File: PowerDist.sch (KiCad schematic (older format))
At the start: 15 parts, among them J3 CarPowerConnector, U2 RI3-1205S, U3 NCP1117-3.3_SOT223

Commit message: Updates dashboard project to most recent version
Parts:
- removed C16: 470pF, Capacitor_SMD:C_2220_5650Metric, symbol Device:C
- removed J3: CarPowerConnector, UTSVT_Connectors:Molex_MicroFit3.0_1x2xP3.00mm_PolarizingPeg_Vertical, symbol utsvt-connectors:CarPowerConnector
- removed L4: SRF0905-100Y, UTSVT_BPS:SRF0905A, symbol utsvt-bps:SRF0905-100Y
- added J18: PowerConn, UTSVT_Connectors:Molex_MicroFit3.0_1x2xP3.00mm_PolarizingPeg_Vertical, symbol Connector_Generic:Conn_01x02
- C20: renamed from C14; value 4.7uF -> 10u; footprint Capacitor_SMD:C_0805_2012Metric -> UTSVT_Passive:C_2220_5750Metric
- C21: renamed from C15; value 0.1uF -> 10u
- C22: renamed from C17; value 10uF -> 10u
- renumbered D1 to D14, R1 to R29, TP1 to TP2, TP2 to TP3, TP3 to TP4, TP4 to TP5, TP5 to TP6, U2 to U12, U3 to U13
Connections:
- wire segments 60 -> 57
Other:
- note added: "+5V is already isolated so no need to isolate +3.3V"
- note added: "ISOLATED"
- note added: "Isolated DC-DC Converter to step down +12V power\nto an isolated +5V. The input gnd (Power GND) is\ndifferent from the output gnd (Local GND)"
- note added: "Linear Regulator to step down +5V to +3.3V.\nAn isolated converter was not used for the +3.3V\nline because of price and space. May need to\nchange this to DC-DC converter if we really\nwant to make the BPS more energy efficient."
- note added: "Local (Leader Board) GND\n(Internal)"
- note added: "Power GND\n(External)"
- note removed: "Two separate converters would cause more noise on the board but less power waste.\nIf too much noise, add 5 to 3.3V regulator.\n"
- moved on the sheet: C20, C21, C22, D14, R29, TP2, TP3, TP4, TP5, TP6, U13

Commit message: Edits schematic to make turn lights software controlled
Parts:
- TP2, TP3, TP4, TP5, TP6: footprint TestPoint:TestPoint_Keystone_5005-5009_Compact -> TestPoint:TestPoint_Pad_1.5x1.5mm
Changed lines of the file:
@@
 $Descr A4 11693 8268
 encoding utf-8
-Sheet 2 6
+Sheet 2 5
 Title ""
 Date ""
@@
 F 0 "TP2" H 3250 3500 50  0000 L CNN
 F 1 "+12V_TP" H 3250 3400 50  0000 L CNN
-F 2 "TestPoint:TestPoint_Keystone_5005-5009_Compact" H 3450 3150 50  0001 C CNN
+F 2 "TestPoint:TestPoint_Pad_1.5x1.5mm" H 3450 3150 50  0001 C CNN
 F 3 "~" H 3450 3150 50  0001 C CNN
 	1    3250 3150
@@
 F 0 "TP4" H 5508 3270 50  0000 L CNN
 F 1 "+5V_TP" H 5508 3179 50  0000 L CNN
-F 2 "TestPoint:TestPoint_Keystone_5005-5009_Compact" H 5650 3150 50  0001 C CNN
+F 2 "TestPoint:TestPoint_Pad_1.5x1.5mm" H 5650 3150 50  0001 C CNN
 F 3 "~" H 5650 3150 50  0001 C CNN
 	1    5450 3150
@@
 F 0 "TP5" H 5392 3727 50  0000 R CNN
 F 1 "GND_TP" H 5392 3818 50  0000 R CNN
-F 2 "TestPoint:TestPoint_Keystone_5005-5009_Compact" H 5650 3700 50  0001 C CNN
+F 2 "TestPoint:TestPoint_Pad_1.5x1.5mm" H 5650 3700 50  0001 C CNN
 F 3 "~" H 5650 3700 50  0001 C CNN
 	1    5450 3700
@@
 F 0 "TP6" H 8808 3270 50  0000 L CNN
 F 1 "+3.3V_TP" H 8800 3350 50  0000 L CNN
-F 2 "TestPoint:TestPoint_Keystone_5005-5009_Compact" H 8950 3150 50  0001 C CNN
+F 2 "TestPoint:TestPoint_Pad_1.5x1.5mm" H 8950 3150 50  0001 C CNN
 F 3 "~" H 8950 3150 50  0001 C CNN
 	1    8750 3150
@@
 F 0 "TP3" H 3192 3677 50  0000 R CNN
 F 1 "GNDPWR_TP" H 3192 3768 50  0000 R CNN
-F 2 "TestPoint:TestPoint_Keystone_5005-5009_Compact" H 3450 3650 50  0001 C CNN
+F 2 "TestPoint:TestPoint_Pad_1.5x1.5mm" H 3450 3650 50  0001 C CNN
 F 3 "~" H 3450 3650 50  0001 C CNN
 	1    3250 3650

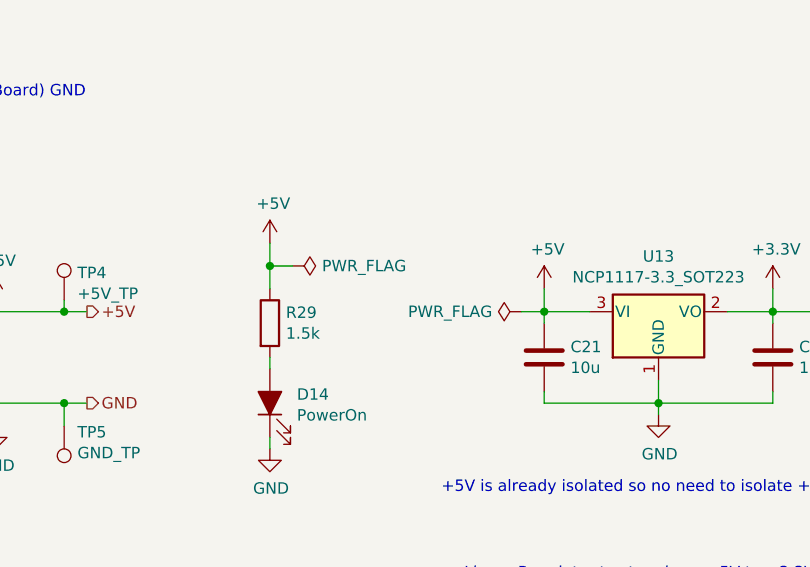
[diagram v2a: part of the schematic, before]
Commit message: Organizes the schematic into hierarchical sheets
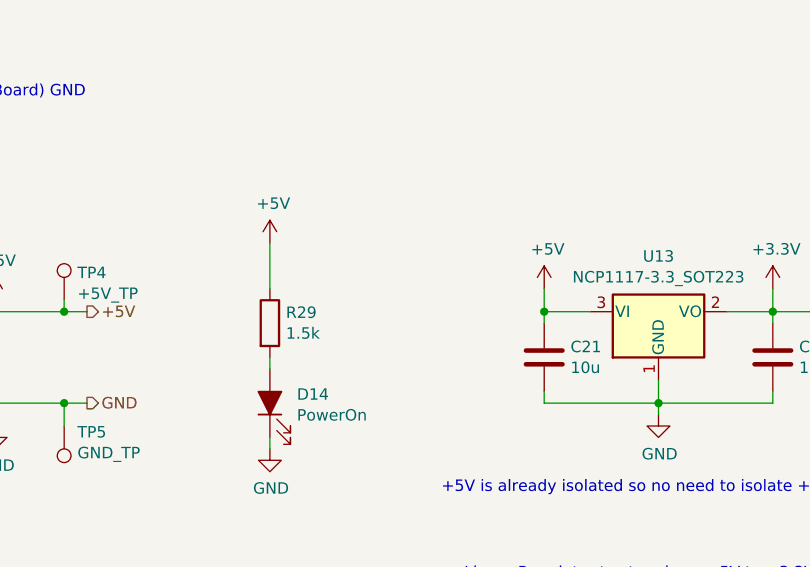
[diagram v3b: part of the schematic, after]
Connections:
- wire segments 57 -> 54
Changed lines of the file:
@@
 $Descr A4 11693 8268
 encoding utf-8
-Sheet 2 5
+Sheet 2 10
 Title ""
 Date ""
@@
 	1    0    0    -1
 $EndComp
-Wire Wire Line
-	6350 2900 6350 3000
 $Comp
 L power:GND #PWR081
@@
 	3000 3200 3000 3350
 $Comp
-L power:PWR_FLAG #FLG04
-U 1 1 5F1E78A7
-P 7450 3200
-F 0 "#FLG04" H 7450 3275 50  0001 C CNN
-F 1 "PWR_FLAG" V 7450 3327 50  0000 L CNN
-F 2 "" H 7450 3200 50  0001 C CNN
-F 3 "~" H 7450 3200 50  0001 C CNN
-	1    7450 3200
-	0    -1   -1   0
-$EndComp
-Wire Wire Line
-	7450 3200 7550 3200
-$Comp
 L power:PWR_FLAG #FLG02
 U 1 1 5F1EAFA2
@@
 	-1   0    0    1
 $EndComp
-$Comp
-L power:PWR_FLAG #FLG03
-U 1 1 5F1ED21F
-P 6450 3000
-F 0 "#FLG03" H 6450 3075 50  0001 C CNN
-F 1 "PWR_FLAG" V 6450 3128 50  0000 L CNN
-F 2 "" H 6450 3000 50  0001 C CNN
-F 3 "~" H 6450 3000 50  0001 C CNN
-	1    6450 3000
-	0    1    1    0
-$EndComp
-Wire Wire Line
-	6450 3000 6350 3000
-Connection ~ 6350 3000
-Wire Wire Line
-	6350 3000 6350 3100
 $Comp
 L power:PWR_FLAG #FLG01
@@
 Wire Wire Line
 	3950 3500 3950 3600
+Wire Wire Line
+	6350 2900 6350 3100
 $EndSCHEMATC

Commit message: USB Tx/Rx, Crystal Keepout, 12V Separation, Can2-Can3, Motor CAN bus labels, Power Input Protection Circuitry
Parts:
- added D6: TVS, Diode_SMD:D_SOD-323, symbol Device:D
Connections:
- wire segments 54 -> 56
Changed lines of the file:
@@
 Wire Wire Line
 	6350 2900 6350 3100
+$Comp
+L Device:D D6
+U 1 1 615A3807
+P 3250 3400
+F 0 "D6" V 3204 3480 50  0000 L CNN
+F 1 "TVS" V 3295 3480 50  0000 L CNN
+F 2 "Diode_SMD:D_SOD-323" H 3250 3400 50  0001 C CNN
+F 3 "~" H 3250 3400 50  0001 C CNN
+	1    3250 3400
+	0    1    1    0
+$EndComp
+Wire Wire Line
+	3250 3250 3250 3200
+Wire Wire Line
+	3250 3550 3250 3600
 $EndSCHEMATC

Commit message: removes the isp
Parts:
- U12: symbol utsvt-power-regulators:RI3-1205S -> Dashboard-rescue:RI3-1205S-utsvt-power-regulators
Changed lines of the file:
@@
 	8750 3200 8550 3200
 $Comp
-L utsvt-power-regulators:RI3-1205S U12
+L Dashboard-rescue:RI3-1205S-utsvt-power-regulators U12
 U 1 1 5C38C4FE
 P 4500 3200

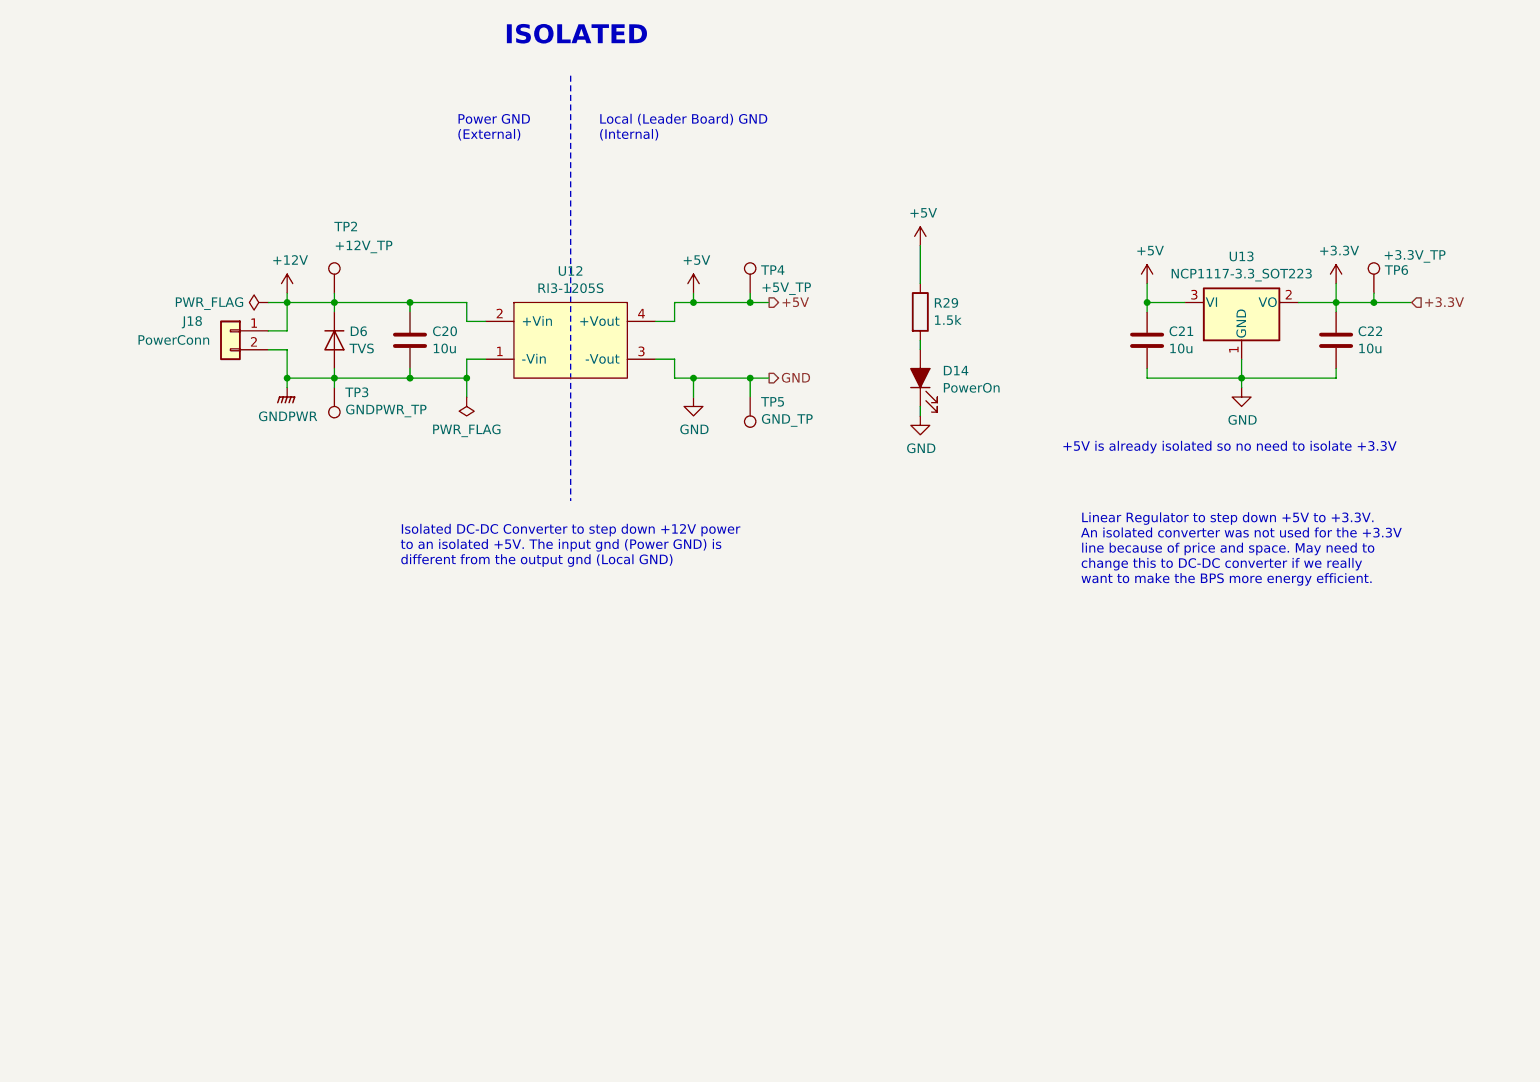
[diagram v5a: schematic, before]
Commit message: Changes the layout of the board, adds resistors for ignition switch, and gives motar can isolated +12v, still need to change resistor value for the isolated +12v(didnt remember how to find the value)
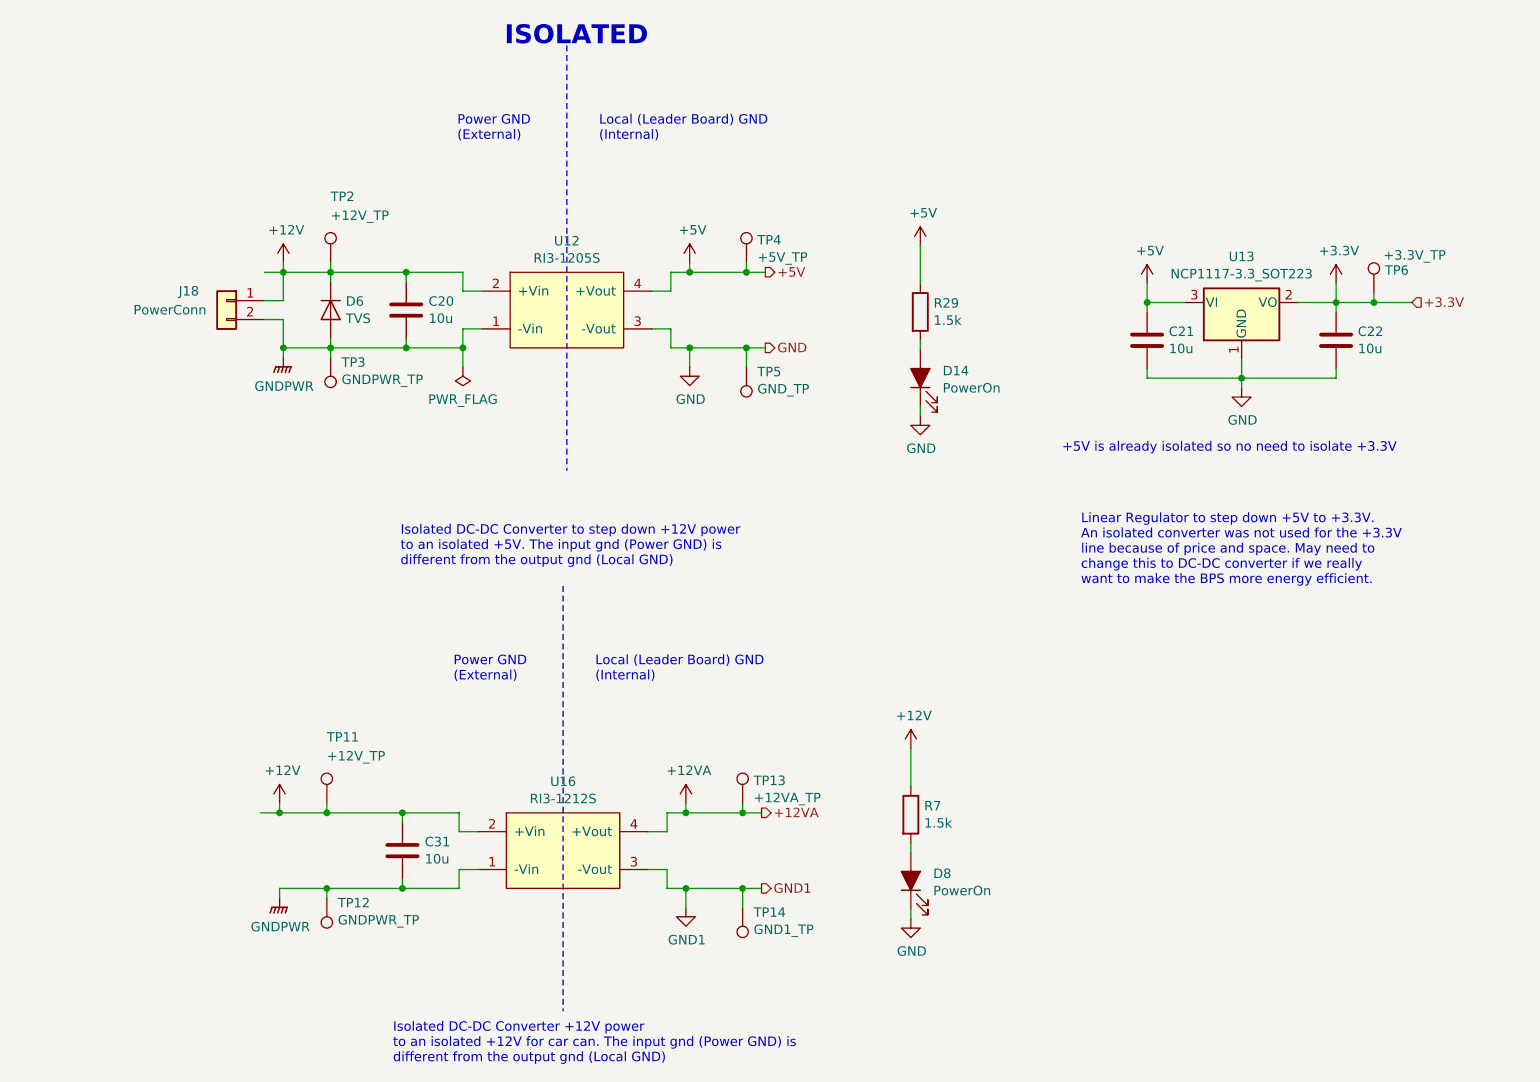
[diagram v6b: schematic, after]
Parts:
- added C31: 10u, UTSVT_Passive:C_2220_5750Metric, symbol Device:C
- added D8: PowerOn, LED_SMD:LED_0805_2012Metric, symbol Device:LED_ALT
- added R7: 1.5k, Resistor_SMD:R_0805_2012Metric, symbol Device:R
- added TP11: +12V_TP, TestPoint:TestPoint_Pad_1.5x1.5mm, symbol Connector:TestPoint
- added TP12: GNDPWR_TP, TestPoint:TestPoint_Pad_1.5x1.5mm, symbol Connector:TestPoint
- added TP13: +12VA_TP, TestPoint:TestPoint_Pad_1.5x1.5mm, symbol Connector:TestPoint
- added TP14: GND1_TP, TestPoint:TestPoint_Pad_1.5x1.5mm, symbol Connector:TestPoint
- added U16: RI3-1212S, UTSVT_ICs:RI3_DC_Converter, symbol Dashboard-rescue:RI3-1205S-utsvt-power-regulators
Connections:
- net +12V: now also C31.1, R7.1, TP11.1, U16.2 (+Vin)
- net GND: now also D8.1 (K)
- net GNDPWR: now also C31.2, TP12.1, U16.1 (-Vin)
- new net: D8.2 (A), R7.2
- new net +12VA: TP13.1, U16.4 (+Vout)
- new net GND1: TP14.1, U16.3 (-Vout)
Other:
- note added: "Isolated DC-DC Converter +12V power\nto an isolated +12V for car can. The input gnd (Power GND) is\ndifferent from the output gnd (Local GND)"
- moved on the sheet: C20, D6, J18, TP2, TP3, TP4, TP5, U12

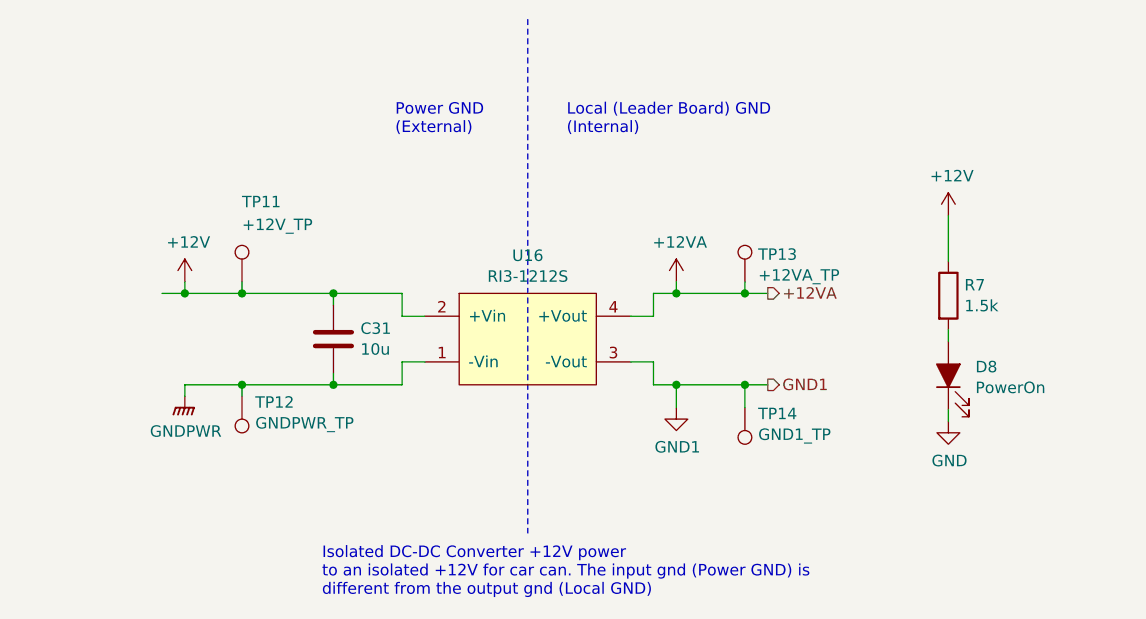
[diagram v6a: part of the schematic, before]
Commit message: Cleans up some of the traces in the power section
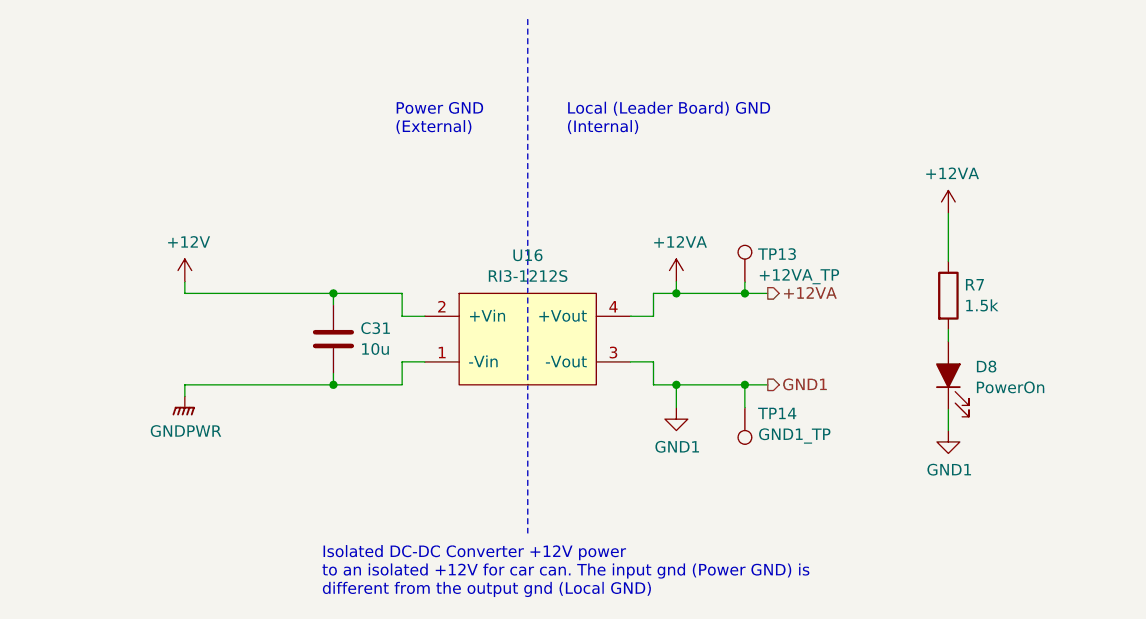
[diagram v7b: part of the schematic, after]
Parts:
- removed TP11: +12V_TP, TestPoint:TestPoint_Pad_1.5x1.5mm, symbol Connector:TestPoint
- removed TP12: GNDPWR_TP, TestPoint:TestPoint_Pad_1.5x1.5mm, symbol Connector:TestPoint
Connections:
- net +12V: no longer R7.1
- net +12VA: now also R7.1
- net GND: no longer D8.1 (K)
- net GND1: now also D8.1 (K)
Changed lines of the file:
@@
 $EndComp
-Wire Wire Line
-	2960 6300 3210 6300
 Wire Wire Line
 	2960 5850 2960 5900
 Wire Wire Line
-	2960 5900 3210 5900
-Connection ~ 2960 5900
-Wire Wire Line
 	3610 5950 3610 5900
-Connection ~ 3210 5900
 Wire Wire Line
 	3610 6250 3610 6300
@@
 	5510 6300 5410 6300
 Connection ~ 5410 6300
-$Comp
-L Connector:TestPoint TP11
-U 1 1 61920B1C
-P 3210 5850
-F 0 "TP11" H 3210 6200 50  0000 L CNN
-F 1 "+12V_TP" H 3210 6100 50  0000 L CNN
-F 2 "TestPoint:TestPoint_Pad_1.5x1.5mm" H 3410 5850 50  0001 C CNN
-F 3 "~" H 3410 5850 50  0001 C CNN
-	1    3210 5850
-	1    0    0    -1
-$EndComp
-Wire Wire Line
-	3210 5850 3210 5900
 Wire Wire Line
 	5410 5850 5410 5900
@@
 Wire Wire Line
 	5410 5900 5510 5900
-$Comp
-L Connector:TestPoint TP12
-U 1 1 61920B4F
-P 3210 6350
-F 0 "TP12" H 3152 6377 50  0000 R CNN
-F 1 "GNDPWR_TP" H 3152 6468 50  0000 R CNN
-F 2 "TestPoint:TestPoint_Pad_1.5x1.5mm" H 3410 6350 50  0001 C CNN
-F 3 "~" H 3410 6350 50  0001 C CNN
-	1    3210 6350
-	-1   0    0    1
-$EndComp
-Wire Wire Line
-	3210 6350 3210 6300
-Wire Wire Line
-	2860 5900 2960 5900
 Text Notes 4630 5210 0    50   ~ 0
 Local (Leader Board) GND\n(Internal)
@@
 Wire Notes Line
 	4460 4700 4460 6950
-Wire Wire Line
-	3210 5900 3610 5900
 Connection ~ 3610 5900
 Wire Wire Line
 	3610 5900 3910 5900
-Wire Wire Line
-	3210 6300 3610 6300
-Connection ~ 3210 6300
-Connection ~ 3610 6300
 Wire Wire Line
 	3610 6300 3910 6300
@@
 Text Notes 3560 7230 0    50   ~ 0
 Isolated DC-DC Converter +12V power\nto an isolated +12V for car can. The input gnd (Power GND) is\ndifferent from the output gnd (Local GND)
-$Comp
-L power:GND #PWR06
-U 1 1 61927CE8
-P 6300 6460
-F 0 "#PWR06" H 6300 6210 50  0001 C CNN
-F 1 "GND" H 6305 6287 50  0000 C CNN
-F 2 "" H 6300 6460 50  0001 C CNN
-F 3 "" H 6300 6460 50  0001 C CNN
-	1    6300 6460
-	1    0    0    -1
-$EndComp
 $Comp
 L Device:LED_ALT D8
@@
 $EndComp
 Wire Wire Line
-	6300 6460 6300 6410
-Wire Wire Line
 	6300 6110 6300 6060
-Wire Wire Line
-	6300 5560 6300 5760
-$Comp
-L power:+12V #PWR05
-U 1 1 6192AEC7
-P 6300 5560
-F 0 "#PWR05" H 6300 5410 50  0001 C CNN
-F 1 "+12V" H 6315 5733 50  0000 C CNN
-F 2 "" H 6300 5560 50  0001 C CNN
-F 3 "" H 6300 5560 50  0001 C CNN
-	1    6300 5560
-	1    0    0    -1
-$EndComp
 Wire Wire Line
 	5010 6300 5110 6300
@@
 $EndComp
 $Comp
-L power:GND1 #PWR013
+L Dashboard-rescue:GND1-power #PWR013
 U 1 1 619CE9D7
 P 5110 6400
+AR Path="/619CE9D7" Ref="#PWR013"  Part="1"
+AR Path="/5F19A9C5/619CE9D7" Ref="#PWR013"  Part="1"
 F 0 "#PWR013" H 5110 6150 50  0001 C CNN
 F 1 "GND1" H 5115 6227 50  0000 C CNN
@@
 	1    0    0    -1
 $EndComp
+$Comp
+L power:+12VA #PWR0132
+U 1 1 61943538
+P 6300 5550
+F 0 "#PWR0132" H 6300 5400 50  0001 C CNN
+F 1 "+12VA" H 6315 5723 50  0000 C CNN
+F 2 "" H 6300 5550 50  0001 C CNN
+F 3 "" H 6300 5550 50  0001 C CNN
+	1    6300 5550
+	1    0    0    -1
+$EndComp
+$Comp
+L Dashboard-rescue:GND1-power #PWR?
+U 1 1 61949364
+P 6300 6500
+AR Path="/61949364" Ref="#PWR?"  Part="1"
+AR Path="/5F19A9C5/61949364" Ref="#PWR0133"  Part="1"
+F 0 "#PWR0133" H 6300 6250 50  0001 C CNN
+F 1 "GND1" H 6305 6327 50  0000 C CNN
+F 2 "" H 6300 6500 50  0001 C CNN
+F 3 "" H 6300 6500 50  0001 C CNN
+	1    6300 6500
+	1    0    0    -1
+$EndComp
+Wire Wire Line
+	6300 6410 6300 6500
+Wire Wire Line
+	6300 5550 6300 5760
+Connection ~ 3610 6300
+Wire Wire Line
+	2960 6300 3610 6300
+Wire Wire Line
+	2960 5900 3610 5900
 $EndSCHEMATC
